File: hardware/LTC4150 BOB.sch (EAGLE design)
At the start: 23 parts, among them U1 LTC4150

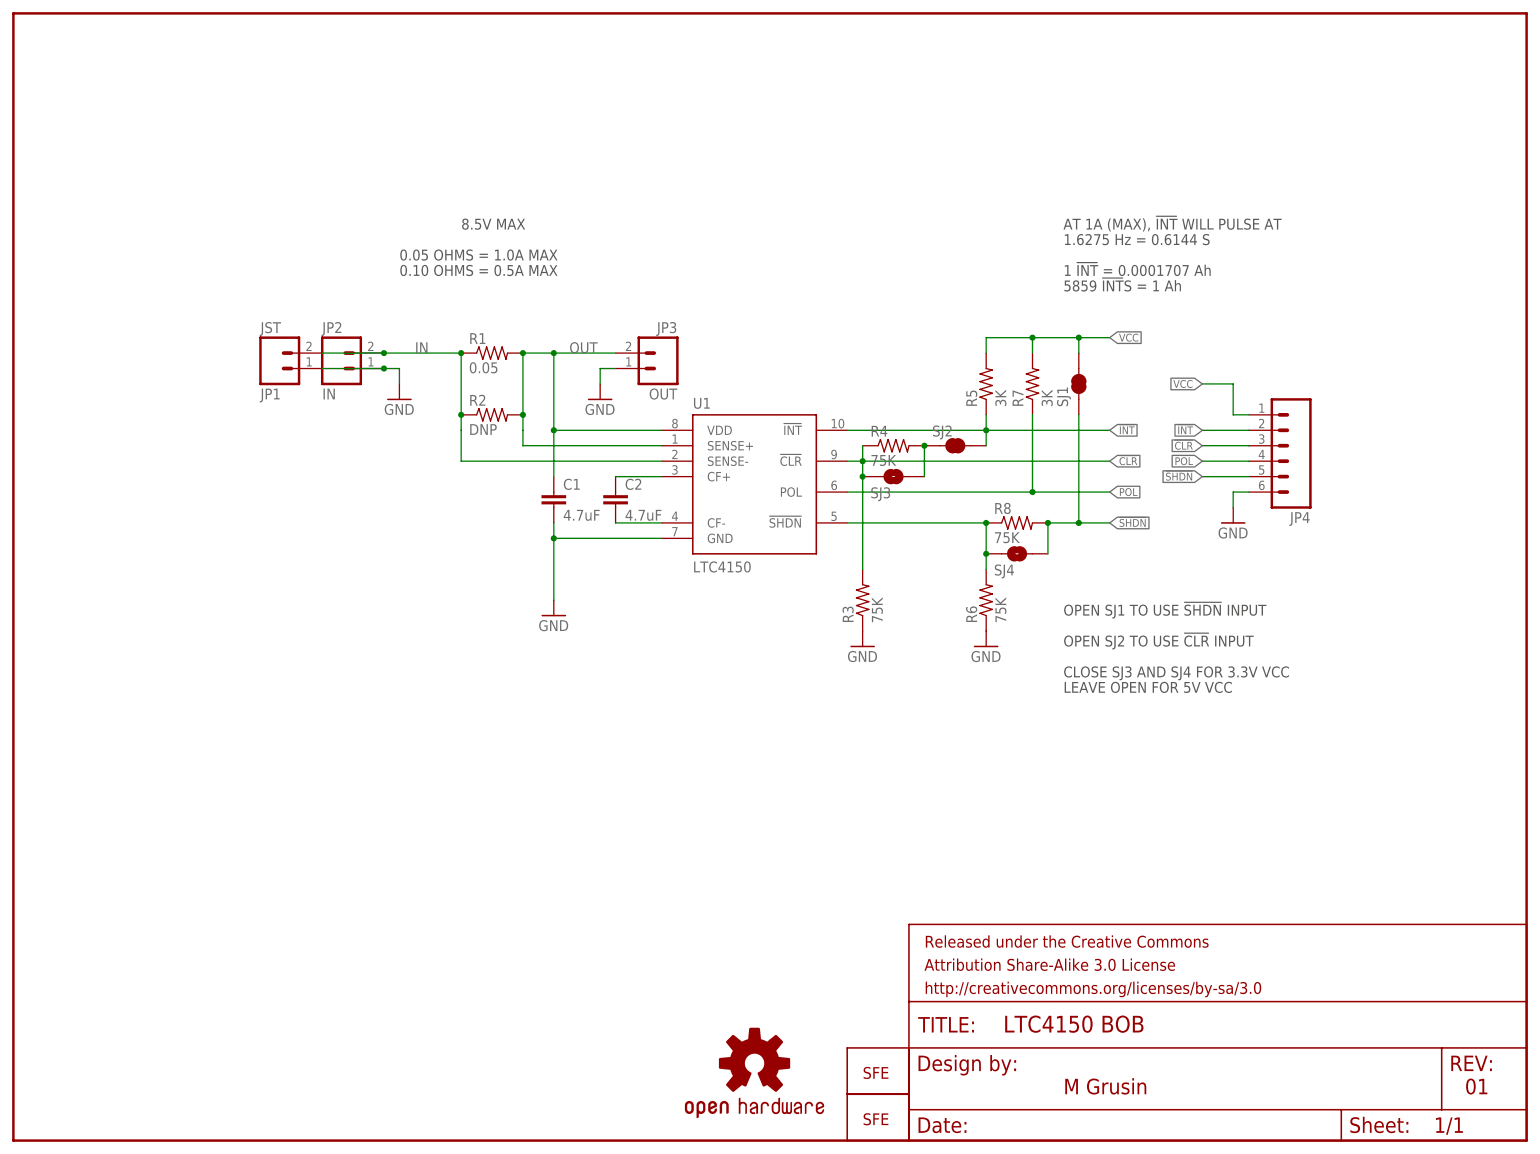
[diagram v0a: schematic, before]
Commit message: V02 ready for prototype
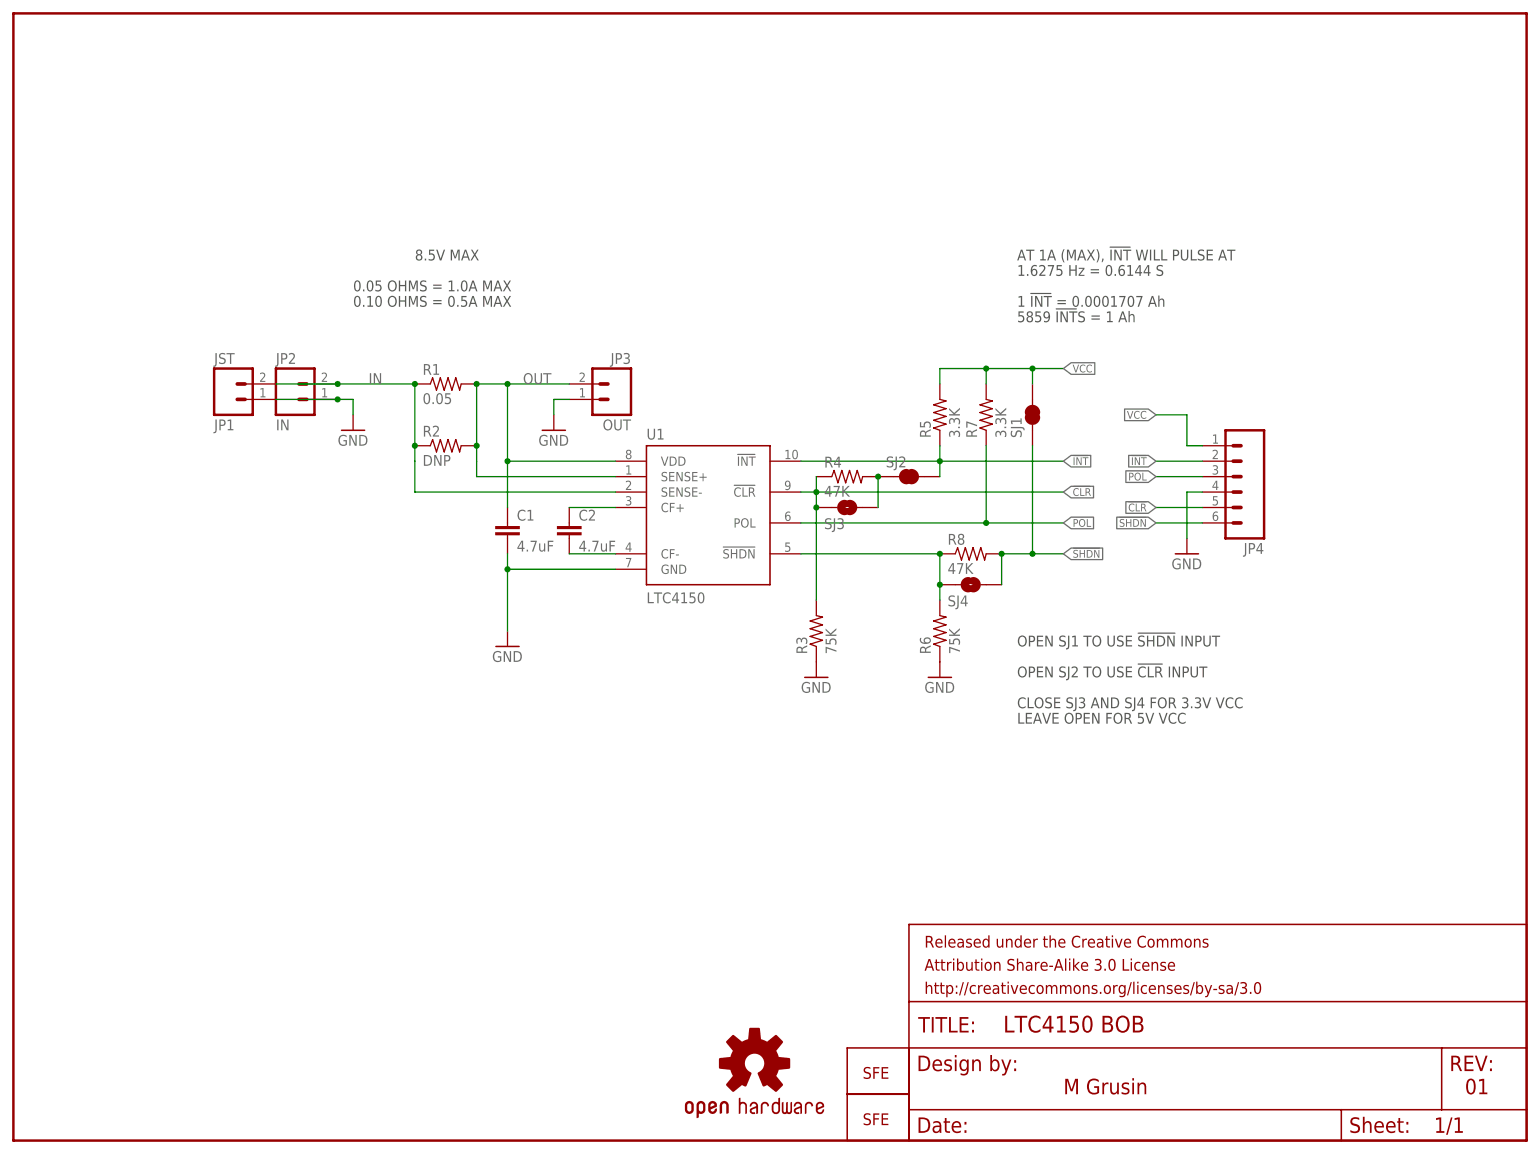
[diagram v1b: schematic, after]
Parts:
- R1: device SparkFun-Passives:RESISTOR0805-RES -> SparkFun-Passives:RESISTOR1206
- R4, R8: value 75K -> 47K
- R5, R7: value 3K -> 3.3K
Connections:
- net !CLR!: now also JP4.5; no longer JP4.3
- net !SHDN!: now also JP4.6; no longer JP4.5
- net GND: now also JP4.4; no longer JP4.6
- net POL: now also JP4.3; no longer JP4.4
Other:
- moved on the sheet: C1, C2, JP1, JP2, JP3, JP4, R1, R2, R3, R4, R5, R6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

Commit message: Final cleanup for reds
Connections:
- net VCC renamed VIO
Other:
- note added: "(SEE SJ3 AND SJ4)"
- note added: "10"
- note added: "CLOSE SJ3 AND SJ4 FOR 3.3V VIO"
- note added: "CURRENT SENSE: 8.5V MAX"
- note added: "LEAVE OPEN FOR 5V VIO"
- note added: "VIO: 3.3V OR 5V"
- note removed: "0.10 OHMS = 0.5A MAX"
- note removed: "01"
- note removed: "8.5V MAX"
- note removed: "CLOSE SJ3 AND SJ4 FOR 3.3V VCC"
- note removed: "LEAVE OPEN FOR 5V VCC"
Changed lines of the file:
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@@
 <grid distance="0.1" unitdist="inch" unit="inch" style="lines" multiple="1" display="no" altdistance="0.01" altunitdist="inch" altunit="inch"/>
 <layers>
-<layer number="1" name="Top" color="4" fill="1" visible="yes" active="no"/>
-<layer number="2" name="Route2" color="1" fill="3" visible="yes" active="no"/>
-<layer number="3" name="Route3" color="4" fill="3" visible="yes" active="no"/>
-<layer number="4" name="Route4" color="1" fill="4" visible="yes" active="no"/>
-<layer number="5" name="Route5" color="4" fill="4" visible="yes" active="no"/>
-<layer number="6" name="Route6" color="1" fill="8" visible="yes" active="no"/>
-<layer number="7" name="Route7" color="4" fill="8" visible="yes" active="no"/>
-<layer number="8" name="Route8" color="1" fill="2" visible="yes" active="no"/>
-<layer number="9" name="Route9" color="4" fill="2" visible="yes" active="no"/>
-<layer number="10" name="Route10" color="1" fill="7" visible="yes" active="no"/>
-<layer number="11" name="Route11" color="4" fill="7" visible="yes" active="no"/>
-<layer number="12" name="Route12" color="1" fill="5" visible="yes" active="no"/>
-<layer number="13" name="Route13" color="4" fill="5" visible="yes" active="no"/>
-<layer number="14" name="Route14" color="1" fill="6" visible="yes" active="no"/>
-<layer number="15" name="Route15" color="4" fill="6" visible="yes" active="no"/>
-<layer number="16" name="Bottom" color="1" fill="1" visible="yes" active="no"/>
-<layer number="17" name="Pads" color="2" fill="1" visible="yes" active="no"/>
-<layer number="18" name="Vias" color="2" fill="1" visible="yes" active="no"/>
-<layer number="19" name="Unrouted" color="6" fill="1" visible="yes" active="no"/>
-<layer number="20" name="Dimension" color="15" fill="1" visible="yes" active="no"/>
-<layer number="21" name="tPlace" color="7" fill="1" visible="yes" active="no"/>
-<layer number="22" name="bPlace" color="7" fill="1" visible="yes" active="no"/>
-<layer number="23" name="tOrigins" color="15" fill="1" visible="yes" active="no"/>
-<layer number="24" name="bOrigins" color="15" fill="1" visible="yes" active="no"/>
-<layer number="25" name="tNames" color="7" fill="1" visible="yes" active="no"/>
-<layer number="26" name="bNames" color="7" fill="1" visible="yes" active="no"/>
-<layer number="27" name="tValues" color="7" fill="1" visible="yes" active="no"/>
-<layer number="28" name="bValues" color="7" fill="1" visible="yes" active="no"/>
+<layer number="1" name="Top" color="4" fill="1" visible="no" active="no"/>
+<layer number="2" name="Route2" color="1" fill="3" visible="no" active="no"/>
+<layer number="3" name="Route3" color="4" fill="3" visible="no" active="no"/>
+<layer number="4" name="Route4" color="1" fill="4" visible="no" active="no"/>
+<layer number="5" name="Route5" color="4" fill="4" visible="no" active="no"/>
+<layer number="6" name="Route6" color="1" fill="8" visible="no" active="no"/>
+<layer number="7" name="Route7" color="4" fill="8" visible="no" active="no"/>
+<layer number="8" name="Route8" color="1" fill="2" visible="no" active="no"/>
+<layer number="9" name="Route9" color="4" fill="2" visible="no" active="no"/>
+<layer number="10" name="Route10" color="1" fill="7" visible="no" active="no"/>
+<layer number="11" name="Route11" color="4" fill="7" visible="no" active="no"/>
+<layer number="12" name="Route12" color="1" fill="5" visible="no" active="no"/>
+<layer number="13" name="Route13" color="4" fill="5" visible="no" active="no"/>
+<layer number="14" name="Route14" color="1" fill="6" visible="no" active="no"/>
+<layer number="15" name="Route15" color="4" fill="6" visible="no" active="no"/>
+<layer number="16" name="Bottom" color="1" fill="1" visible="no" active="no"/>
+<layer number="17" name="Pads" color="2" fill="1" visible="no" active="no"/>
+<layer number="18" name="Vias" color="2" fill="1" visible="no" active="no"/>
+<layer number="19" name="Unrouted" color="6" fill="1" visible="no" active="no"/>
+<layer number="20" name="Dimension" color="15" fill="1" visible="no" active="no"/>
+<layer number="21" name="tPlace" color="7" fill="1" visible="no" active="no"/>
+<layer number="22" name="bPlace" color="7" fill="1" visible="no" active="no"/>
+<layer number="23" name="tOrigins" color="15" fill="1" visible="no" active="no"/>
+<layer number="24" name="bOrigins" color="15" fill="1" visible="no" active="no"/>
+<layer number="25" name="tNames" color="7" fill="1" visible="no" active="no"/>
+<layer number="26" name="bNames" color="7" fill="1" visible="no" active="no"/>
+<layer number="27" name="tValues" color="7" fill="1" visible="no" active="no"/>
+<layer number="28" name="bValues" color="7" fill="1" visible="no" active="no"/>
 <layer number="29" name="tStop" color="7" fill="3" visible="no" active="no"/>
 <layer number="30" name="bStop" color="7" fill="6" visible="no" active="no"/>
@@
 <layer number="35" name="tGlue" color="7" fill="4" visible="no" active="no"/>
 <layer number="36" name="bGlue" color="7" fill="5" visible="no" active="no"/>
-<layer number="37" name="tTest" color="7" fill="1" visible="yes" active="no"/>
-<layer number="38" name="bTest" color="7" fill="1" visible="yes" active="no"/>
+<layer number="37" name="tTest" color="7" fill="1" visible="no" active="no"/>
+<layer number="38" name="bTest" color="7" fill="1" visible="no" active="no"/>
 <layer number="39" name="tKeepout" color="4" fill="11" visible="no" active="no"/>
 <layer number="40" name="bKeepout" color="1" fill="11" visible="no" active="no"/>
@@
 <layer number="44" name="Drills" color="7" fill="1" visible="no" active="no"/>
 <layer number="45" name="Holes" color="7" fill="1" visible="no" active="no"/>
-<layer number="46" name="Milling" color="3" fill="1" visible="yes" active="no"/>
-<layer number="47" name="Measures" color="7" fill="1" visible="yes" active="no"/>
-<layer number="48" name="Document" color="7" fill="1" visible="yes" active="no"/>
-<layer number="49" name="Reference" color="7" fill="1" visible="yes" active="no"/>
-<layer number="50" name="dxf" color="7" fill="1" visible="yes" active="no"/>
-<layer number="51" name="tDocu" color="7" fill="1" visible="yes" active="no"/>
-<layer number="52" name="bDocu" color="7" fill="1" visible="yes" active="no"/>
-<layer number="53" name="tGND_GNDA" color="7" fill="9" visible="yes" active="no"/>
-<layer number="54" name="bGND_GNDA" color="1" fill="9" visible="yes" active="no"/>
-<layer number="56" name="wert" color="7" fill="1" visible="yes" active="no"/>
+<layer number="46" name="Milling" color="3" fill="1" visible="no" active="no"/>
+<layer number="47" name="Measures" color="7" fill="1" visible="no" active="no"/>
+<layer number="48" name="Document" color="7" fill="1" visible="no" active="no"/>
+<layer number="49" name="Reference" color="7" fill="1" visible="no" active="no"/>
+<layer number="50" name="dxf" color="7" fill="1" visible="no" active="no"/>
+<layer number="51" name="tDocu" color="7" fill="1" visible="no" active="no"/>
+<layer number="52" name="bDocu" color="7" fill="1" visible="no" active="no"/>
+<layer number="53" name="tGND_GNDA" color="7" fill="9" visible="no" active="no"/>
+<layer number="54" name="bGND_GNDA" color="1" fill="9" visible="no" active="no"/>
+<layer number="56" name="wert" color="7" fill="1" visible="no" active="no"/>
 <layer number="91" name="Nets" color="2" fill="1" visible="yes" active="yes"/>
 <layer number="92" name="Busses" color="1" fill="1" visible="yes" active="yes"/>
@@
 <plain>
 <text x="172.72" y="7.62" size="2.54" layer="94">M Grusin</text>
-<text x="238.76" y="7.62" size="2.54" layer="94">01</text>
-<text x="165.1" y="71.12" size="1.778" layer="97">CLOSE SJ3 AND SJ4 FOR 3.3V VCC</text>
+<text x="238.76" y="7.62" size="2.54" layer="94">10</text>
+<text x="165.1" y="71.12" size="1.778" layer="97">CLOSE SJ3 AND SJ4 FOR 3.3V VIO</text>
 <text x="165.1" y="81.28" size="1.778" layer="97">OPEN SJ1 TO USE !SHDN! INPUT</text>
-<text x="66.04" y="144.78" size="1.778" layer="97">8.5V MAX</text>
-<text x="165.1" y="68.58" size="1.778" layer="97">LEAVE OPEN FOR 5V VCC</text>
+<text x="55.88" y="144.78" size="1.778" layer="97">CURRENT SENSE: 8.5V MAX</text>
+<text x="165.1" y="68.58" size="1.778" layer="97">LEAVE OPEN FOR 5V VIO</text>
 <text x="165.1" y="144.78" size="1.778" layer="97">AT 1A (MAX), !INT! WILL PULSE AT</text>
 <text x="165.1" y="142.24" size="1.778" layer="97">1.6275 Hz = 0.6144 S</text>
@@
 <rectangle x1="167.132" y1="118.364" x2="168.148" y2="120.142" layer="94"/>
 <text x="55.88" y="139.7" size="1.778" layer="97">0.05 OHMS = 1.0A MAX</text>
-<text x="55.88" y="137.16" size="1.778" layer="97">0.10 OHMS = 0.5A MAX</text>
+<text x="190.5" y="127" size="1.778" layer="97">VIO: 3.3V OR 5V</text>
+<text x="190.5" y="124.46" size="1.778" layer="97">(SEE SJ3 AND SJ4)</text>
 </plain>
 <instances>
@@
 <instance part="GND1" gate="1" x="132.08" y="76.2"/>
 <instance part="GND2" gate="1" x="152.4" y="76.2"/>
-<instance part="GND3" gate="1" x="81.28" y="81.28"/>
+<instance part="GND3" gate="1" x="81.28" y="86.36"/>
 <instance part="JP1" gate="G$1" x="35.56" y="124.46" rot="MR180"/>
 <instance part="JP2" gate="G$1" x="45.72" y="121.92"/>
@@
 <wire x1="99.06" y1="93.98" x2="81.28" y2="93.98" width="0.1524" layer="91"/>
 <wire x1="81.28" y1="93.98" x2="81.28" y2="96.52" width="0.1524" layer="91"/>
-<wire x1="81.28" y1="93.98" x2="81.28" y2="83.82" width="0.1524" layer="91"/>
+<wire x1="81.28" y1="93.98" x2="81.28" y2="88.9" width="0.1524" layer="91"/>
 <junction x="81.28" y="93.98"/>
 <pinref part="GND3" gate="1" pin="GND"/>
@@
 </segment>
 </net>
-<net name="VCC" class="0">
+<net name="VIO" class="0">
 <segment>
 <pinref part="R5" gate="G$1" pin="2"/>
